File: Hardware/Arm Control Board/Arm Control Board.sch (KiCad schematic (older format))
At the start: 15 parts

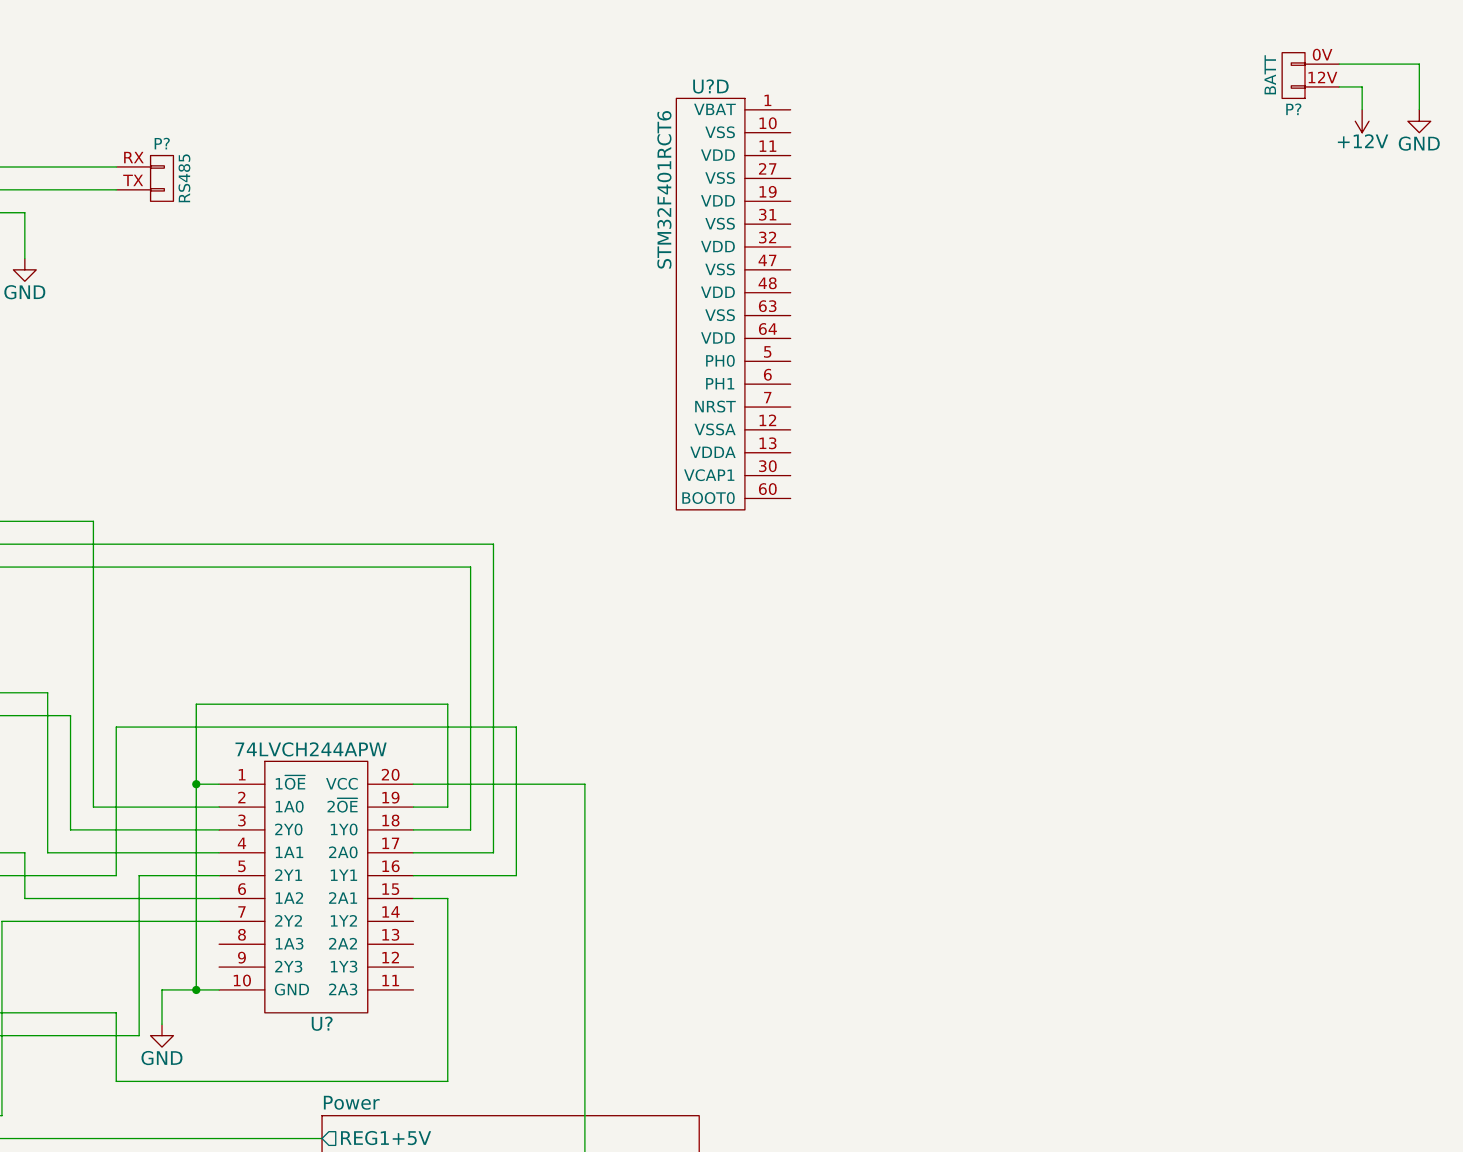
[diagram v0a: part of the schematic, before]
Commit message: Cleaned up schematic, cube, added stepper connector
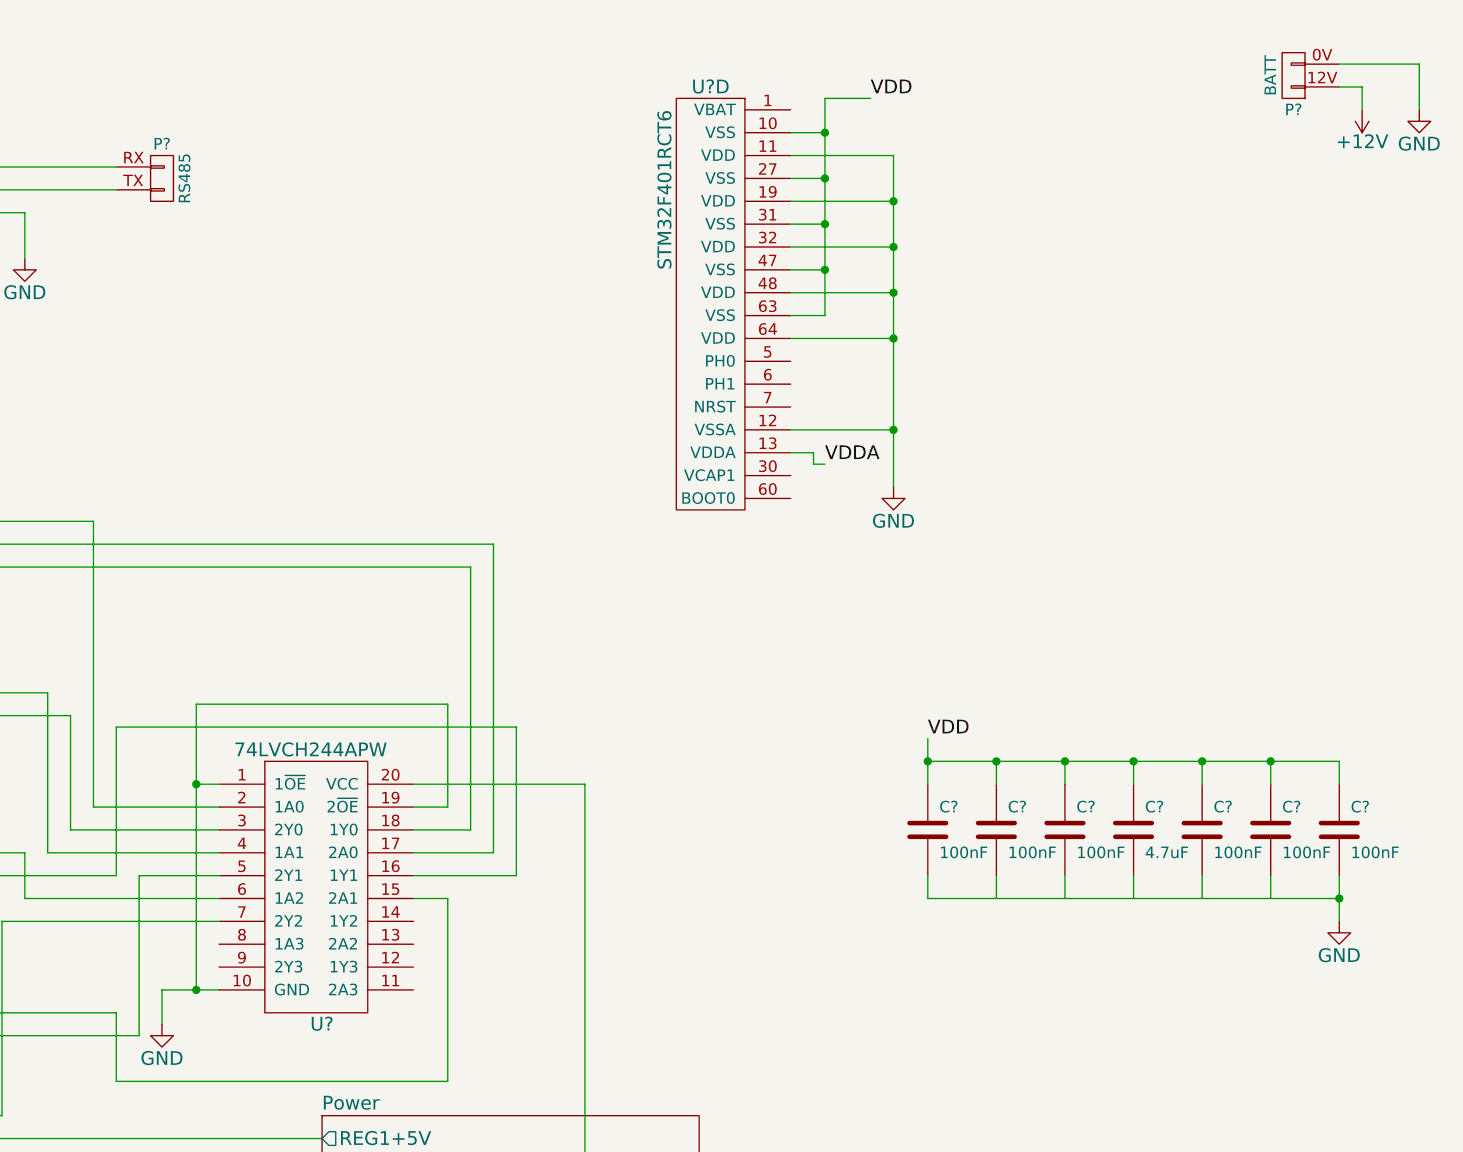
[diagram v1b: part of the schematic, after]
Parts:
- added C? (x6): 100nF, symbol C
- added C?: 4.7uF, symbol C
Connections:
- net labels added: VDD, VDDA
- wire segments 111 -> 144
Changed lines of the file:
@@
 	5750 3900 5000 3900
 Wire Wire Line
-	4150 4800 3900 4800
+	3900 4800 4150 4800
 Wire Wire Line
 	3900 4800 3900 4950
@@
 	5150 3550 4050 3550
 Connection ~ 4050 3900
+Wire Wire Line
+	6650 1150 7100 1150
+Wire Wire Line
+	7100 1150 7100 2600
+Wire Wire Line
+	6650 1950 7100 1950
+Connection ~ 7100 1950
+Wire Wire Line
+	6650 1750 7100 1750
+Connection ~ 7100 1750
+Wire Wire Line
+	6650 1550 7100 1550
+Connection ~ 7100 1550
+Wire Wire Line
+	6650 1350 7100 1350
+Connection ~ 7100 1350
+$Comp
+L GND #PWR?
+U 1 1 54CA71B9
+P 7100 2600
+F 0 "#PWR?" H 7100 2350 60  0001 C CNN
+F 1 "GND" H 7100 2450 60  0000 C CNN
+F 2 "" H 7100 2600 60  0000 C CNN
+F 3 "" H 7100 2600 60  0000 C CNN
+	1    7100 2600
+	1    0    0    -1
+$EndComp
+Wire Wire Line
+	6650 1250 6800 1250
+Wire Wire Line
+	6800 900  6800 1850
+Wire Wire Line
+	6800 900  7000 900
+Wire Wire Line
+	6800 1850 6650 1850
+Connection ~ 6800 1250
+Wire Wire Line
+	6650 1650 6800 1650
+Connection ~ 6800 1650
+Wire Wire Line
+	6650 1450 6800 1450
+Connection ~ 6800 1450
+Text Label 7000 900  0    60   ~ 0
+VDD
+$Comp
+L C C?
+U 1 1 54CA8C27
+P 7250 4100
+F 0 "C?" H 7300 4200 50  0000 L CNN
+F 1 "100nF" H 7300 4000 50  0000 L CNN
+F 2 "" H 7288 3950 30  0000 C CNN
+F 3 "" H 7250 4100 60  0000 C CNN
+	1    7250 4100
+	1    0    0    -1
+$EndComp
+$Comp
+L C C?
+U 1 1 54CA8D66
+P 7550 4100
+F 0 "C?" H 7600 4200 50  0000 L CNN
+F 1 "100nF" H 7600 4000 50  0000 L CNN
+F 2 "" H 7588 3950 30  0000 C CNN
+F 3 "" H 7550 4100 60  0000 C CNN
+	1    7550 4100
+	1    0    0    -1
+$EndComp
+$Comp
+L C C?
+U 1 1 54CA8D93
+P 7850 4100
+F 0 "C?" H 7900 4200 50  0000 L CNN
+F 1 "100nF" H 7900 4000 50  0000 L CNN
+F 2 "" H 7888 3950 30  0000 C CNN
+F 3 "" H 7850 4100 60  0000 C CNN
+	1    7850 4100
+	1    0    0    -1
+$EndComp
+$Comp
+L C C?
+U 1 1 54CA8DC5
+P 8450 4100
+F 0 "C?" H 8500 4200 50  0000 L CNN
+F 1 "100nF" H 8500 4000 50  0000 L CNN
+F 2 "" H 8488 3950 30  0000 C CNN
+F 3 "" H 8450 4100 60  0000 C CNN
+	1    8450 4100
+	1    0    0    -1
+$EndComp
+$Comp
+L C C?
+U 1 1 54CA8E07
+P 8750 4100
+F 0 "C?" H 8800 4200 50  0000 L CNN
+F 1 "100nF" H 8800 4000 50  0000 L CNN
+F 2 "" H 8788 3950 30  0000 C CNN
+F 3 "" H 8750 4100 60  0000 C CNN
+	1    8750 4100
+	1    0    0    -1
+$EndComp
+$Comp
+L C C?
+U 1 1 54CA8E37
+P 9050 4100
+F 0 "C?" H 9100 4200 50  0000 L CNN
+F 1 "100nF" H 9100 4000 50  0000 L CNN
+F 2 "" H 9088 3950 30  0000 C CNN
+F 3 "" H 9050 4100 60  0000 C CNN
+	1    9050 4100
+	1    0    0    -1
+$EndComp
+$Comp
+L C C?
+U 1 1 54CA9993
+P 8150 4100
+F 0 "C?" H 8200 4200 50  0000 L CNN
+F 1 "4.7uF" H 8200 4000 50  0000 L CNN
+F 2 "" H 8188 3950 30  0000 C CNN
+F 3 "" H 8150 4100 60  0000 C CNN
+	1    8150 4100
+	1    0    0    -1
+$EndComp
+Wire Wire Line
+	7250 4300 7250 4400
+Wire Wire Line
+	7550 4300 7550 4400
+Wire Wire Line
+	7850 4300 7850 4400
+Wire Wire Line
+	8150 4300 8150 4400
+Wire Wire Line
+	8450 4300 8450 4400
+Wire Wire Line
+	8750 4300 8750 4400
+$Comp
+L GND #PWR?
+U 1 1 54CAB654
+P 9050 4500
+F 0 "#PWR?" H 9050 4250 60  0001 C CNN
+F 1 "GND" H 9050 4350 60  0000 C CNN
+F 2 "" H 9050 4500 60  0000 C CNN
+F 3 "" H 9050 4500 60  0000 C CNN
+	1    9050 4500
+	1    0    0    -1
+$EndComp
+Wire Wire Line
+	9050 3800 9050 3900
+Wire Wire Line
+	7250 3800 9050 3800
+Wire Wire Line
+	7250 3700 7250 3900
+Connection ~ 7250 3800
+Wire Wire Line
+	7550 3800 7550 3900
+Connection ~ 7550 3800
+Wire Wire Line
+	7850 3800 7850 3900
+Connection ~ 7850 3800
+Wire Wire Line
+	8150 3800 8150 3900
+Connection ~ 8150 3800
+Wire Wire Line
+	8450 3800 8450 3900
+Connection ~ 8450 3800
+Wire Wire Line
+	8750 3800 8750 3900
+Connection ~ 8750 3800
+Text Label 7250 3700 0    60   ~ 0
+VDD
+Text Label 6800 2500 0    60   ~ 0
+VDDA
+Wire Wire Line
+	6650 2350 7100 2350
+Connection ~ 7100 2350
+Wire Wire Line
+	7250 4400 9050 4400
+Wire Wire Line
+	9050 4300 9050 4500
+Connection ~ 9050 4400
+Wire Wire Line
+	6650 2450 6750 2450
+Wire Wire Line
+	6750 2450 6750 2500
+Wire Wire Line
+	6750 2500 6800 2500
+Wire Wire Line
+	6650 1050 6800 1050
+Connection ~ 6800 1050
 $EndSCHEMATC

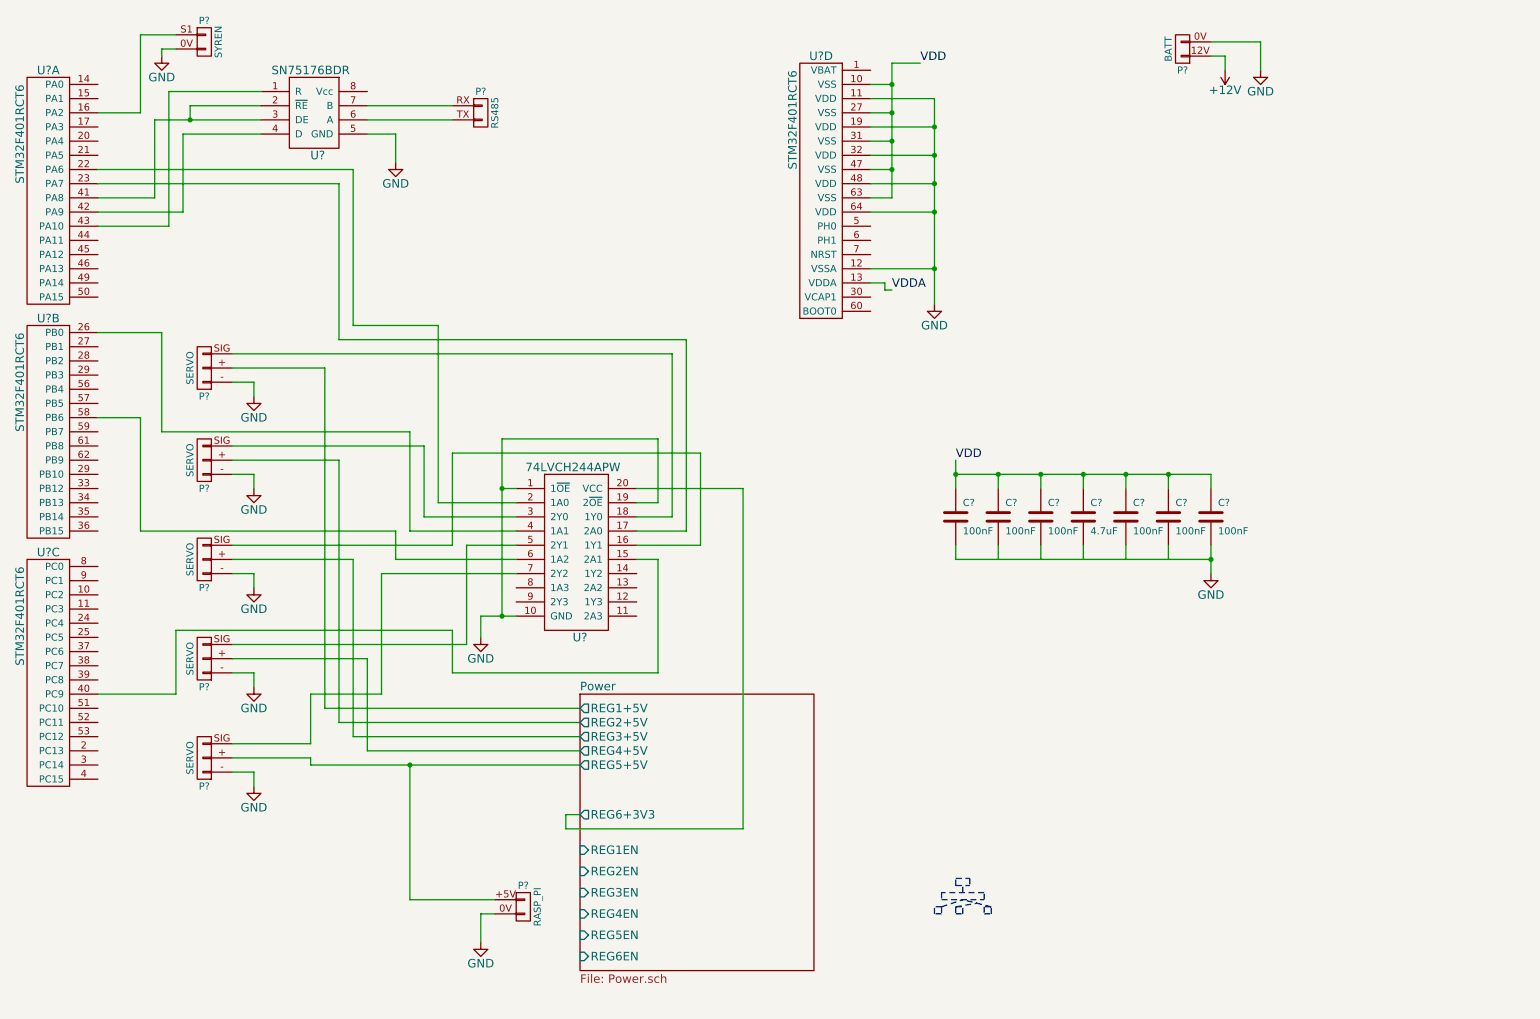
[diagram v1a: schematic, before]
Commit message: More clean up, added connector for actuator fbck
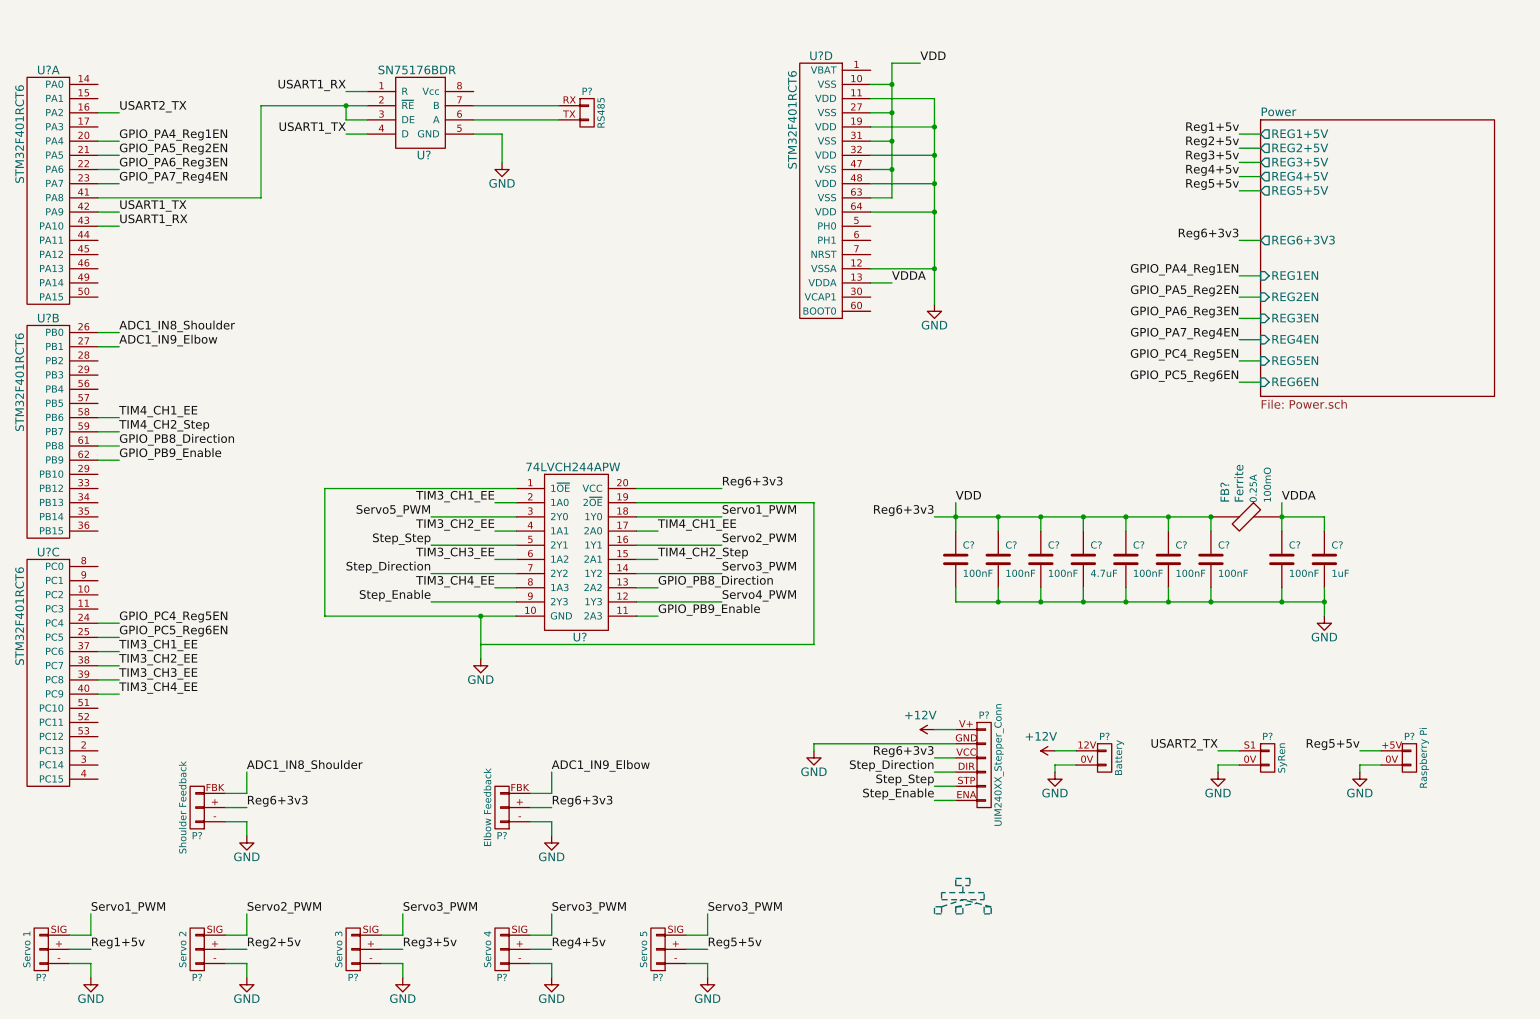
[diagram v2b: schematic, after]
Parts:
- added C?: 100nF, symbol C
- added C?: 1uF, symbol C
- added FB?: Ferrite, symbol Ferrite
- added P?: UIM240XX_Stepper_Conn, symbol UIM240XX_Conn
- added P?: Shoulder Feedback, symbol Actuator_Pot
- added P?: Elbow Feedback, symbol Actuator_Pot
- P?: value BATT -> Battery
- P?: value SERVO -> Servo 1
- P?: value SERVO -> Servo 2
- P?: value SERVO -> Servo 3
- P?: value SERVO -> Servo 4
- P?: value SERVO -> Servo 5
- P?: value SYREN -> SyRen
- P?: value RASP_PI -> Raspberry Pi
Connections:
- net labels added: ADC1_IN8_Shoulder, ADC1_IN9_Elbow, GPIO_PA4_Reg1EN, GPIO_PA5_Reg2EN, GPIO_PA6_Reg3EN, GPIO_PA7_Reg4EN, GPIO_PB8_Direction, GPIO_PB9_Enable, GPIO_PC4_Reg5EN, GPIO_PC5_Reg6EN, Reg1+5v, Reg2+5v, Reg3+5v, Reg4+5v, Reg5+5v, Reg6+3v3, Servo1_PWM, Servo2_PWM, Servo3_PWM, Servo4_PWM, Servo5_PWM, Step_Direction, Step_Enable, Step_Step, TIM3_CH1_EE, TIM3_CH2_EE, TIM3_CH3_EE, TIM3_CH4_EE, TIM4_CH1_EE, TIM4_CH2_Step, USART1_RX, USART1_TX, USART2_TX
- wire segments 144 -> 180
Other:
- moved on the sheet: C?, P?, U?

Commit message: Added SWD connector for program/debug
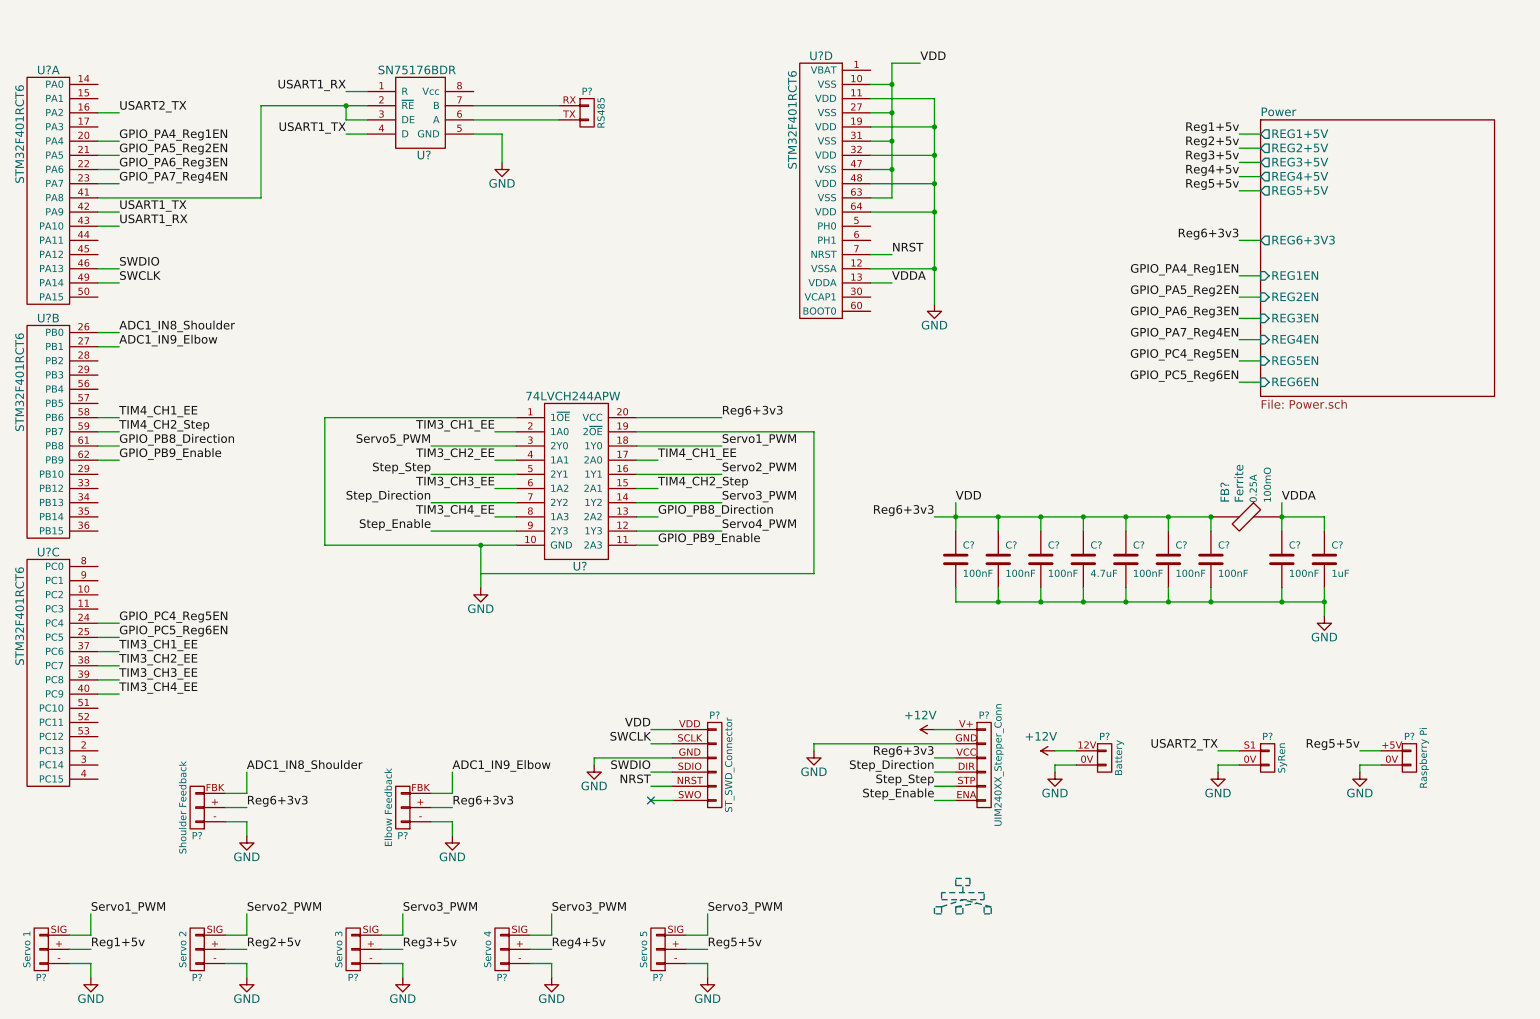
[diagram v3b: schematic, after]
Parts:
- added P?: ST_SWD_Connector, symbol ST_SWD_Connector
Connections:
- net GND: now also P?.GND
- net Reg6+3v3: now also P?.VDD (VDD_TARGET)
- net SWDIO: now reaches U?.46 (PA13)
- net SWDIO: now also P?.SDIO (SWDIO)
- net SWCLK: now reaches U?.49 (PA14)
- net SWCLK: now also P?.SCLK (SWCLK)
- net NRST: now reaches U?.7 (NRST)
- net NRST: now also P?.NRST
- no-connect marks 0 -> 1
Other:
- moved on the sheet: P?, U?
